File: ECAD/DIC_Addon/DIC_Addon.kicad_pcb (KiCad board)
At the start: 2 copper layers, 67.9 x 50.2 mm, 63 parts, among them J2 Conn_01x06_Pin, J3 Conn_01x06_Pin, J4 Conn_01x06_Pin, J5 Conn_01x06_Pin, Q1 FDN352AP, Q10 2N7002, Q11 2N7002, Q12 2N7002, Q2 FDN352AP, Q3 FDN352AP, Q4 FDN352AP, Q5 2N7002, Q6 2N7002, Q7 2N7002, Q8 2N7002, Q9 2N7002, U1 Thebe-II

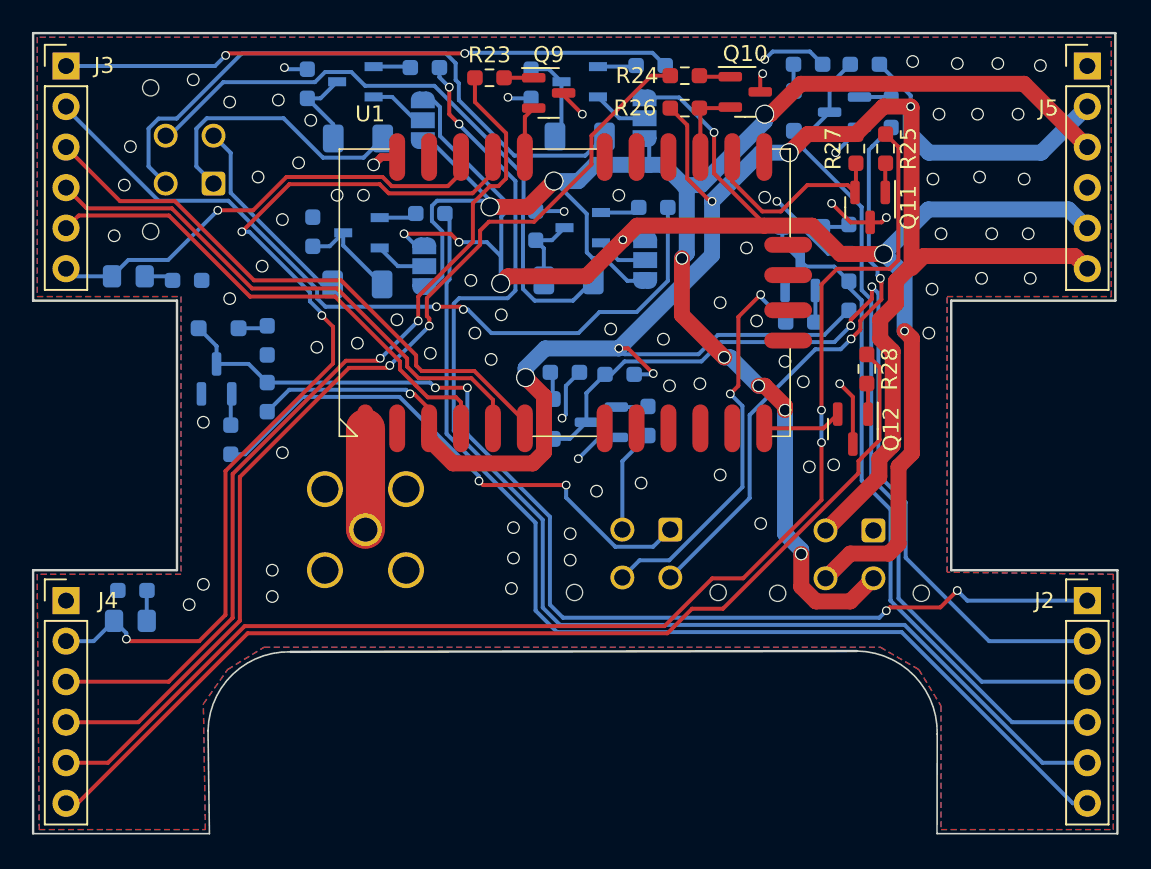
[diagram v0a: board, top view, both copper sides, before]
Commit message: switch to ribbon cable pcb interconnect
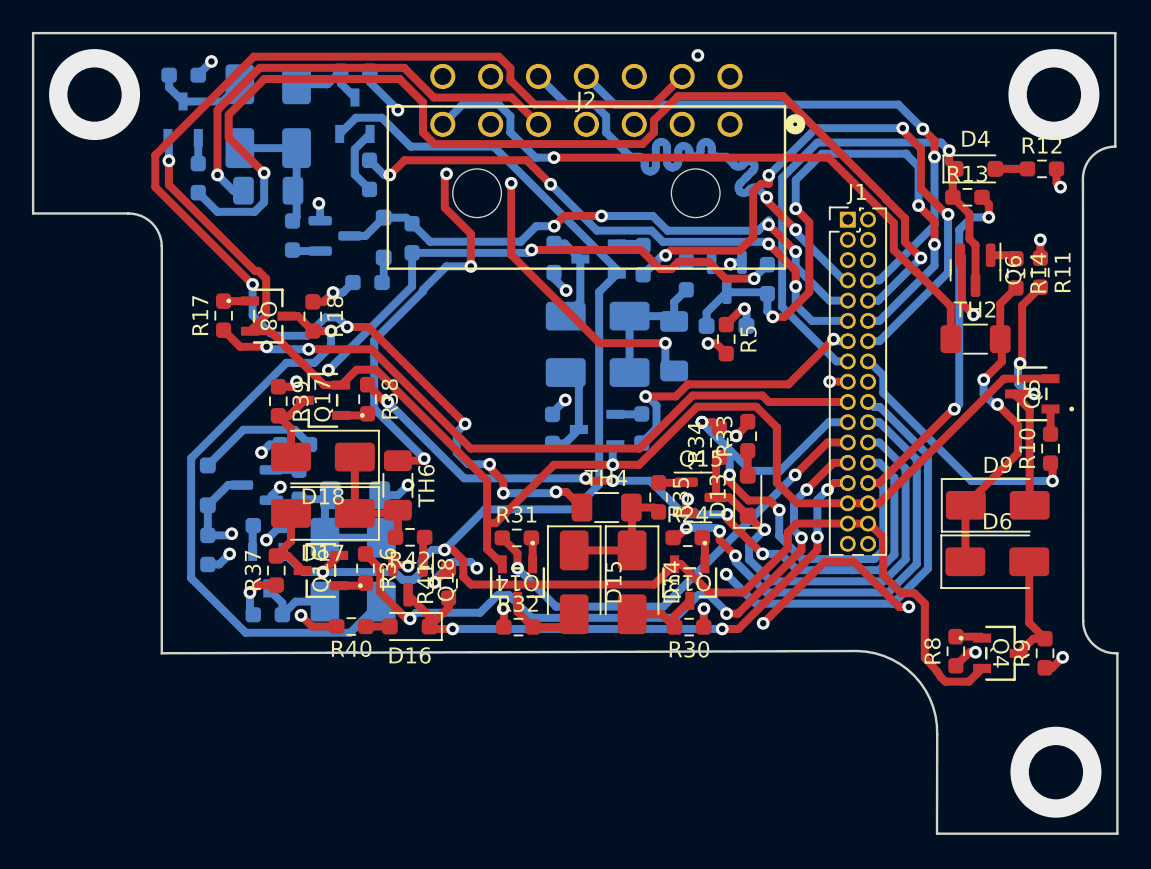
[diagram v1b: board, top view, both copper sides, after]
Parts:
- removed 868Mhz: Conn_Coaxial, Connector_Coaxial:SMA_Wurth_60312002114503_Vertical
- removed EXT_Power1, GPI1, GPO1: Micro-Fit_3.0_43045-0412, Lukas:Molex_Micro-Fit_3.0_43045-0412_2x02_P3.00mm_Vertical
- removed J3, J4, J5: Conn_01x06_Pin, Connector_PinHeader_2.54mm:PinHeader_1x06_P2.54mm_Vertical
- removed JP1, JP2, JP3, JP4: Jumper_3_Open, Jumper:SolderJumper-3_P1.3mm_Open_RoundedPad1.0x1.5mm_NumberLabels
- removed Radio_RX1, Radio_TX1: LED Blue, LED_SMD:LED_0805_2012Metric_Pad1.15x1.40mm_HandSolder
- removed U1: Thebe-II, Lukas:Thebe-II
- added D10: Z 3.3V, Diode_SMD:D_SOD-323_HandSoldering, B.Cu at (22.9, 40.3)
- added D11: B120-13-F, Diode_SMD:D_SMA, B.Cu at (30.2, 45.6)
- added D12: B120-13-F, Diode_SMD:D_SMA, B.Cu at (33.8, 45.6)
- added D13: Z 3.3V, Diode_SMD:D_SOD-323_HandSoldering, F.Cu at (56.7, 40.9)
- added D14: B120-13-F, Diode_SMD:D_SMA, F.Cu at (49.5, 46.4)
- added D15: B120-13-F, Diode_SMD:D_SMA, F.Cu at (45.8, 46.4)
- added D16: Z 3.3V, Diode_SMD:D_SOD-323_HandSoldering, F.Cu at (35.5, 49.1)
- added D17: B120-13-F, Diode_SMD:D_SMA, F.Cu at (30.1, 42.0)
- added D18: B120-13-F, Diode_SMD:D_SMA, F.Cu at (30.1, 38.5)
- added D5: Z 3.3V, Diode_SMD:D_SOD-323_HandSoldering, B.Cu at (33.9, 24.8)
- added D6: B120-13-F, Diode_SMD:D_SMA, F.Cu at (72.4, 45.1)
- added D7: B120-13-F, Diode_SMD:D_SMA, B.Cu at (28.4, 17.1)
- added D8: B120-13-F, Diode_SMD:D_SMA, B.Cu at (24.9, 17.1)
- added D9: B120-13-F, Diode_SMD:D_SMA, F.Cu at (72.4, 41.5)
- added J1: WE 62702621621, Connector_PinHeader_1.27mm:PinHeader_2x17_P1.27mm_Vertical, F.Cu at (63.0, 23.6)
- added Q13: FDN352AP, Lukas:SOT23_527AG_ONS, F.Cu at (53.1, 46.4)
- added Q14: FDN352AP, Lukas:SOT23_527AG_ONS, F.Cu at (42.3, 46.4)
- added Q15: 2N7002, Package_TO_SOT_SMD:SOT-23, F.Cu at (53.8, 41.0)
- added Q16: FDN352AP, Lukas:SOT23_527AG_ONS, F.Cu at (30.0, 45.6)
- added Q17: FDN352AP, Lukas:SOT23_527AG_ONS, F.Cu at (30.1, 34.9)
- added Q18: 2N7002, Package_TO_SOT_SMD:SOT-23, F.Cu at (35.4, 46.2)
- added R29: 1kR 0603, Resistor_SMD:R_0603_1608Metric_Pad0.98x0.95mm_HandSolder, B.Cu at (28.2, 24.6)
- added R30: 10kR 0603, Resistor_SMD:R_0603_1608Metric_Pad0.98x0.95mm_HandSolder, F.Cu at (53.0, 49.2)
- added R31: 1kR 0603, Resistor_SMD:R_0603_1608Metric_Pad0.98x0.95mm_HandSolder, F.Cu at (42.2, 43.6)
- added R32: 10kR 0603, Resistor_SMD:R_0603_1608Metric_Pad0.98x0.95mm_HandSolder, F.Cu at (42.4, 49.2)
- added R33: 100R 0603, Resistor_SMD:R_0603_1608Metric_Pad0.98x0.95mm_HandSolder, F.Cu at (56.7, 37.2)
- added R34: 1kR 0603, Resistor_SMD:R_0603_1608Metric_Pad0.98x0.95mm_HandSolder, F.Cu at (54.9, 37.6)
- added R35: 1kR 0603, Resistor_SMD:R_0603_1608Metric_Pad0.98x0.95mm_HandSolder, F.Cu at (51.1, 41.0)
- added R36: 1kR 0603, Resistor_SMD:R_0603_1608Metric_Pad0.98x0.95mm_HandSolder, F.Cu at (32.8, 45.5)
- added R37: 10kR 0603, Resistor_SMD:R_0603_1608Metric_Pad0.98x0.95mm_HandSolder, F.Cu at (27.2, 45.6)
- added R38: 1kR 0603, Resistor_SMD:R_0603_1608Metric_Pad0.98x0.95mm_HandSolder, F.Cu at (32.9, 34.9)
- added R39: 10kR 0603, Resistor_SMD:R_0603_1608Metric_Pad0.98x0.95mm_HandSolder, F.Cu at (27.3, 35.0)
- added R40: 100R 0603, Resistor_SMD:R_0603_1608Metric_Pad0.98x0.95mm_HandSolder, F.Cu at (31.9, 49.1)
- added R41: 1kR 0603, Resistor_SMD:R_0603_1608Metric_Pad0.98x0.95mm_HandSolder, F.Cu at (38.0, 46.4)
- added R42: 1kR 0603, Resistor_SMD:R_0603_1608Metric_Pad0.98x0.95mm_HandSolder, F.Cu at (35.6, 43.5)
- added TH5: SMD1206B025TF, Resistor_SMD:R_1206_3216Metric_Pad1.30x1.75mm_HandSolder, B.Cu at (26.7, 21.8)
- added TH6: SMD1206B025TF, Resistor_SMD:R_1206_3216Metric_Pad1.30x1.75mm_HandSolder, F.Cu at (34.8, 40.3)
- D2, D3: value Z 3.3V -> B120-13-F; footprint Diode_SMD:D_SOD-323_HandSoldering -> Diode_SMD:D_SMA
- D4, Q4, Q6, R12, R13, R14, R17: moved to F.Cu
- J2: value Conn_01x06_Pin -> 430451400; footprint Connector_PinHeader_2.54mm:PinHeader_1x06_P2.54mm_Vertical -> Lukas:CONN_SD-43045-001_14_MOL
- Q10, Q12, R25, R28: moved to B.Cu
- Q11, Q9: value 2N7002 -> FDN352AP; footprint Package_TO_SOT_SMD:SOT-23 -> Lukas:SOT23_527AG_ONS; moved to B.Cu
- Q3: value FDN352AP -> 2N7002; footprint Lukas:SOT23_527AG_ONS -> Package_TO_SOT_SMD:SOT-23
- Q5, Q8: value 2N7002 -> FDN352AP; footprint Package_TO_SOT_SMD:SOT-23 -> Lukas:SOT23_527AG_ONS; moved to F.Cu
- Q7: value 2N7002 -> FDN352AP; footprint Package_TO_SOT_SMD:SOT-23 -> Lukas:SOT23_527AG_ONS
- R10: value 100R 0603 -> 1kR 0603; moved to F.Cu
- R11, R9: value 100R 0603 -> 10kR 0603; moved to F.Cu
- R16, R2, R4: value 1kR 0603 -> 10kR 0603
- R18: value 1kR 0603 -> 10kR 0603; moved to F.Cu
- R19: value 1kR 0603 -> 100R 0603
- R21, R22: value 180R 0603 -> 1kR 0603
- R23, R27: value 1kR 0603 -> 10kR 0603; moved to B.Cu
- R26: value 1kR 0603 -> 100R 0603; moved to B.Cu
- R5: value 10kR 0603 -> 100R 0603; moved to F.Cu
- R6, R7: value 10kR 0603 -> 1kR 0603
- R8: value 10kR 0603 -> 1kR 0603; moved to F.Cu
- TH1, TH3: value SMD1206B050TF/15 -> SMD1206B025TF
- TH2, TH4: value SMD1206B050TF/15 -> SMD1206B025TF; moved to F.Cu
- moved R9 52.5 mm to (75.3, 50.8), turned to 90 degrees
- moved Q5 51.1 mm to (74.5, 34.5)
- moved R15 47.3 mm to (26.6, 42.8), turned to 180 degrees
- moved Q7 46.2 mm to (26.6, 45.6), turned to 0 degrees
- moved R13 45.6 mm to (70.5, 22.2), turned to 0 degrees
- moved Q11 43.4 mm to (21.3, 17.4), turned to 180 degrees
- moved R25 43.1 mm to (22.3, 21.0), turned to 90 degrees
- moved R19 42.8 mm to (28.3, 37.7), turned to 180 degrees
- moved R27 42.4 mm to (21.4, 14.6), turned to 180 degrees
- moved R16 41.5 mm to (26.6, 48.4), turned to 0 degrees
- moved R20 39.8 mm to (22.9, 44.3), turned to -90 degrees
- moved Q10 39.3 mm to (25.9, 40.3), turned to 180 degrees
- moved TH2 38.9 mm to (71.0, 31.1)
- moved R8 37.5 mm to (69.8, 50.7), turned to 90 degrees
- moved Q4 37.4 mm to (72.6, 50.8)
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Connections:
- D1 pad 1: GPI1_CTRL -> GPIO2_In
- D2 pad 1: GPI2_CTRL -> Net-(D2-K)
- D3 pad 1: GPI3_CTRL -> Net-(D2-K)
- D4 pad 1: GPI4_CTRL -> GPIO3_In
- J2 pad 1: GPI1_CTRL -> Analog1_In
- J2 pad 2: GPI2_CTRL -> Analog0_In
- J2 pad 3: GPI3_CTRL -> Analog2_In
- J2 pad 4: GPI4_CTRL -> Analog3_In
- J2 pad 5: GPO1_CTRL -> GPIO1_out/in
- J2 pad 6: GPO2_CTRL -> GPIO2_out/in
- Q1 pad 2: Net-(JP1-C) -> +12V
- Q1 pad 3: Net-(Q1-D) -> Net-(D2-A)
- Q10 pad 2: Net-(Q10-S) -> GND
- Q10 pad 3: GND -> GPIO4_In
- Q11 pad 2: Net-(Q11-S) -> +5V
- Q11 pad 3: GND -> Net-(D8-A)
- Q12 pad 2: Net-(Q12-S) -> GND
- Q12 pad 3: GND -> GPIO1_In
- Q2 pad 2: Net-(JP2-C) -> +5V
- Q2 pad 3: Net-(Q2-D) -> Net-(D3-A)
- Q3 pad 2: Net-(JP3-C) -> GND
- Q3 pad 3: Net-(Q3-D) -> GPIO2_In
- Q4 pad 2: Net-(JP4-C) -> +12V
- Q4 pad 3: Net-(Q4-D) -> Net-(D6-A)
- Q5 pad 2: GND -> +5V
- Q5 pad 3: GPI1_CTRL -> Net-(D9-A)
- Q6 pad 3: GPI2_CTRL -> GPIO3_In
- Q7 pad 2: GND -> +12V
- Q7 pad 3: GPI3_CTRL -> Net-(D11-A)
- Q8 pad 2: GND -> +5V
- Q8 pad 3: GPI4_CTRL -> Net-(D12-A)
- Q9 pad 2: Net-(Q9-S) -> +12V
- Q9 pad 3: GND -> Net-(D7-A)
- R1 pad 1: GPO1_CTRL -> GPIO2_12VOut
- R10 pad 1: Net-(D2-A) -> GPIO3_5VOut
- R10 pad 2: GND -> Net-(Q5-G)
- R11 pad 1: Net-(D3-A) -> GND
- R11 pad 2: GND -> Net-(D9-A)
- R13 pad 1: GPI1_CTRL -> GPIO3_In
- R14 pad 1: GPI2_CTRL -> Net-(Q6-G)
- R14 pad 2: +3.3V -> Net-(D6-K)
- R15 pad 1: GPI3_CTRL -> GPIO4_12VOut
- R15 pad 2: +3.3V -> Net-(Q7-G)
- R16 pad 1: GPI4_CTRL -> GND
- R16 pad 2: +3.3V -> Net-(D11-A)
- R17 pad 1: Net-(Q5-G) -> GPIO4_5VOut
- R17 pad 2: GPI1 -> Net-(Q8-G)
- R18 pad 1: Net-(Q6-G) -> GND
- R18 pad 2: GPI2 -> Net-(D12-A)
- R19 pad 1: Net-(Q7-G) -> Net-(D10-A)
- R19 pad 2: GPI3 -> GND
- R2 pad 1: GPO2_CTRL -> GND
- R2 pad 2: Net-(Q2-G) -> Net-(D2-A)
- R20 pad 1: Net-(Q8-G) -> GPIO4_In
- R20 pad 2: GPI4 -> +3.3V
- R21 pad 1: Net-(Radio_TX1-K) -> GPIO1_12VOut
- R21 pad 2: GND -> Net-(Q9-G)
- R22 pad 1: GND -> Net-(Q10-G)
- R22 pad 2: Net-(Radio_RX1-K) -> Net-(D11-K)
- R23 pad 1: Radio_RESET -> GND
- R23 pad 2: Net-(Q9-G) -> Net-(D7-A)
- R24 pad 1: Mode_1 -> GPIO5_12VOut
- R24 pad 2: Net-(Q10-G) -> Net-(Q13-G)
- R25 pad 1: Wake-Up -> GPIO1_5VOut
- R26 pad 1: Net-(Q10-S) -> Net-(D5-A)
- R26 pad 2: +3.3V -> GND
- R27 pad 1: Net-(Q11-S) -> GND
- R27 pad 2: +3.3V -> Net-(D8-A)
- R28 pad 1: Radio_BOOT -> GPIO1_In
- R28 pad 2: Net-(Q12-G) -> +3.3V
- R3 pad 1: GPO3_CTRL -> GPIO2_5VOut
- R3 pad 2: Net-(Q3-G) -> Net-(Q2-G)
- R4 pad 1: GPO4_CTRL -> GND
- R4 pad 2: Net-(Q4-G) -> Net-(D3-A)
- R5 pad 1: GND -> Net-(D1-A)
- R5 pad 2: Net-(Q1-D) -> GND
- R6 pad 1: GND -> GPIO2_In
- R6 pad 2: Net-(Q2-D) -> +3.3V
- R7 pad 1: GND -> Net-(Q3-G)
- R7 pad 2: Net-(Q3-D) -> Net-(D2-K)
- R8 pad 1: GND -> GPIO3_12VOut
- R8 pad 2: Net-(Q4-D) -> Net-(Q4-G)
- R9 pad 1: Net-(D1-A) -> GND
- R9 pad 2: GND -> Net-(D6-A)
- TH1 pad 1: GPO1 -> GPIO2_out/in
- TH1 pad 2: Net-(Q1-D) -> Net-(D2-K)
- TH2 pad 1: GPO2 -> GPIO3_out/in
- TH2 pad 2: Net-(Q2-D) -> Net-(D6-K)
- TH3 pad 1: GPO3 -> GPIO4_out/in
- TH3 pad 2: Net-(Q3-D) -> Net-(D11-K)
- TH4 pad 1: GPO4 -> GPIO5_out/in
- TH4 pad 2: Net-(Q4-D) -> Net-(D14-K)
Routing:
- net +12V: track 0.00 -> 107.2 mm, vias 0 -> 2
- net Wake-Up: track 81.4 -> 0.00 mm, vias 2 -> 0
- net GPO1_CTRL: track 79.7 -> 0.00 mm, vias 2 -> 0
- net GPIO5_out/in: track 0.00 -> 79.6 mm, vias 0 -> 6
- net +BATT: track 103.2 -> 30.0 mm, vias 7 -> 0
- net GPIO4_In: track 0.00 -> 70.1 mm, vias 0 -> 3
- net GPI1_CTRL: track 69.8 -> 0.00 mm, vias 4 -> 0
- net GPIO1_5VOut: track 0.00 -> 69.6 mm, vias 0 -> 2
- net GPO2_CTRL: track 67.0 -> 0.00 mm
- net Radio_BOOT: track 66.5 -> 0.00 mm
- net Mode_1: track 62.7 -> 0.00 mm, vias 2 -> 0
- net RX_IND: track 60.2 -> 0.00 mm, vias 3 -> 0
- net GPIO4_12VOut: track 0.00 -> 59.1 mm, vias 0 -> 2
- net GPI2_CTRL: track 57.1 -> 0.00 mm, vias 2 -> 0
- net Radio_RESET: track 55.3 -> 0.00 mm, vias 2 -> 0
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- added copper zone on In1.Cu, net GND
- added copper zone on In2.Cu, net GND
- removed copper zone on B.Cu, net GND
- removed copper zone on F.Cu, net GND
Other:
- outline, holes or cut-outs redrawn
- copper layers 2 -> 4

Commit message: finisjed PCB projekt
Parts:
- removed J1: WE 62702621621, Connector_PinHeader_1.27mm:PinHeader_2x17_P1.27mm_Vertical
- added J3: WE 62702621621, Connector_PinHeader_1.27mm:PinHeader_2x08_P1.27mm_Vertical, B.Cu at (50.6, 23.9)
- added J4: Conn_02x05_Top_Bottom, Connector_PinSocket_1.27mm:PinSocket_2x05_P1.27mm_Vertical, F.Cu at (75.8, 54.5)
- added J5: Conn_02x05_Top_Bottom, Connector_PinSocket_1.27mm:PinSocket_2x05_P1.27mm_Vertical, F.Cu at (16.1, 20.7)
- added J6: Conn_02x05_Top_Bottom, Connector_PinSocket_1.27mm:PinSocket_2x05_P1.27mm_Vertical, F.Cu at (16.9, 54.5)
- J2: value 430451400 -> Conn_02x05_Top_Bottom; footprint Lukas:CONN_SD-43045-001_14_MOL -> Connector_PinSocket_1.27mm:PinSocket_2x05_P1.27mm_Vertical
- Q8, R17, R18, R5: moved to B.Cu
- moved R27 60.7 mm to (75.9, 41.3), turned to 0 degrees
- moved Q11 58.5 mm to (75.9, 38.5), turned to 0 degrees
- moved R25 54.5 mm to (75.0, 34.8), turned to -90 degrees
- moved D8 52.2 mm to (72.4, 38.7), turned to -90 degrees
- moved D7 45.8 mm to (68.8, 38.7), turned to -90 degrees
- moved TH5 45.6 mm to (70.6, 34.0), turned to 180 degrees
- moved R12 45.6 mm to (29.9, 15.1), turned to 180 degrees
- moved R23 42.8 mm to (65.2, 41.5), turned to 0 degrees
- moved R29 41.4 mm to (69.1, 31.2), turned to -90 degrees
- moved D4 40.2 mm to (30.9, 18.3), turned to 90 degrees
- moved R11 39.8 mm to (37.4, 14.2), turned to 0 degrees
- moved Q9 39.5 mm to (65.2, 38.7), turned to 0 degrees
- moved R9 39.5 mm to (61.2, 13.9), turned to 180 degrees
- moved R13 38.0 mm to (32.6, 18.8), turned to 90 degrees
- moved R14 37.8 mm to (37.4, 15.7), turned to 0 degrees
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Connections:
- J2 pad 1: Analog1_In -> CAN1_N
- J2 pad 10: GPIO6_out/in -> Analog3_In
- J2 pad 2: Analog0_In -> CAN1_P
- J2 pad 3: Analog2_In -> Analog0_In
- J2 pad 4: Analog3_In -> GND
- J2 pad 5: GPIO1_out/in -> GND
- J2 pad 6: GPIO2_out/in -> Analog1_In
- J2 pad 7: GPIO3_out/in -> GND
- J2 pad 8: GPIO4_out/in -> Analog2_In
- J2 pad 9: GPIO5_out/in -> GND
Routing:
- net GPIO5_out/in: track 79.6 -> 33.7 mm, vias 6 -> 2
- net +5V: track 87.9 -> 130.4 mm, vias 2 -> 8
- net +BATT: track 30.0 -> 65.5 mm
- net GPIO4_In: track 70.1 -> 35.0 mm, vias 3 -> 2
- net GPIO3_out/in: track 41.2 -> 6.78 mm, vias 1 -> 0
- net GPIO4_out/in: track 53.5 -> 19.3 mm
- net GPIO3_5VOut: track 16.5 -> 46.1 mm
- net GPIO3_12VOut: track 27.6 -> 57.0 mm
- net GPIO4_12VOut: track 59.1 -> 30.2 mm
- net GPIO4_5VOut: track 43.7 -> 16.5 mm
- net GPIO2_12VOut: track 39.1 -> 14.1 mm, vias 4 -> 0
- net GPIO5_In: track 28.4 -> 52.8 mm
- net GPIO5_12VOut: track 29.0 -> 49.7 mm
- net +3.3V: track 142.4 -> 122.1 mm
- net GPIO1_12VOut: track 36.1 -> 56.3 mm, vias 4 -> 5
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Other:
- board size 67.9 x 50.2 mm -> 67.9 x 50.3 mm

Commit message: few small changes
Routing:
- net GPIO3_In: track 32.7 -> 31.1 mm
- net GPIO3_5VOut: track 46.1 -> 45.1 mm
- net GPIO3_12VOut: track 57.0 -> 56.4 mm

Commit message: production ready
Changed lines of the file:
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@@
     (property "ki_keywords" "FDN352AP")
     (attr smd)
-    (fp_text reference "Q14" (at 2.5608 -0.8858 unlocked) (layer "F.SilkS")
+    (fp_text reference "Q14" (at 0 0 -90 unlocked) (layer "F.SilkS")
         (effects (font (size 1 1) (thickness 0.15)))
     )
@@
     (property "ki_keywords" "FDN352AP")
     (attr smd)
-    (fp_text reference "Q16" (at -2.9752 -3.302 unlocked) (layer "F.SilkS")
+    (fp_text reference "Q16" (at 0 0 unlocked) (layer "F.SilkS")
         (effects (font (size 1 1) (thickness 0.15)))
     )
@@
     (property "ki_keywords" "FDN352AP")
     (attr smd)
-    (fp_text reference "Q13" (at -3.4082 0.0286 -90 unlocked) (layer "F.SilkS")
+    (fp_text reference "Q13" (at 0 0 -90 unlocked) (layer "F.SilkS")
         (effects (font (size 1 1) (thickness 0.15)))
     )
@@
     (property "ki_keywords" "FDN352AP")
     (attr smd)
-    (fp_text reference "Q17" (at 3.2732 -0.0254 unlocked) (layer "F.SilkS")
+    (fp_text reference "Q17" (at 0 0 unlocked) (layer "F.SilkS")
         (effects (font (size 1 1) (thickness 0.15)))
     )
@@
     (property "ki_keywords" "FDN352AP")
     (attr smd)
-    (fp_text reference "Q5" (at -1.524 -1.9056 unlocked) (layer "F.SilkS")
+    (fp_text reference "Q5" (at 0 0 180 unlocked) (layer "F.SilkS")
         (effects (font (size 1 1) (thickness 0.15)))
     )
@@
     (property "ki_keywords" "FDN352AP")
     (attr smd)
-    (fp_text reference "Q4" (at -2.7432 0.0133 unlocked) (layer "F.SilkS")
+    (fp_text reference "Q4" (at 0 0 unlocked) (layer "F.SilkS")
         (effects (font (size 1 1) (thickness 0.15)))
     )
@@
     (property "ki_keywords" "R res resistor")
     (attr smd)
-    (fp_text reference "R16" (at 30.918401 -44.303101) (layer "B.SilkS")
+    (fp_text reference "R16" (at 1.563 1.225 90) (layer "B.SilkS")
         (effects (font (size 1 1) (thickness 0.15)) (justify mirror))
     )
@@
     (property "ki_keywords" "FDN352AP")
     (attr smd)
-    (fp_text reference "Q9" (at -2.745901 -0.9906 -180 unlocked) (layer "B.SilkS")
+    (fp_text reference "Q9" (at 0 0 180 unlocked) (layer "B.SilkS")
         (effects (font (size 1 1) (thickness 0.15)) (justify mirror))
     )
-    (fp_text value "FDN352AP" (at 0 0 -180 unlocked) (layer "B.Fab")
+    (fp_text value "FDN352AP" (at 0 0 180 unlocked) (layer "B.Fab")
         (effects (font (size 1 1) (thickness 0.15)) (justify mirror))
     )
-    (fp_text user "${REFERENCE}" (at 0 0 -180 unlocked) (layer "B.Fab")
+    (fp_text user "${REFERENCE}" (at 0 0 180 unlocked) (layer "B.Fab")
         (effects (font (size 1 1) (thickness 0.15)) (justify mirror))
     )
@@
     (property "ki_keywords" "FDN352AP")
     (attr smd)
-    (fp_text reference "Q7" (at -2.4418 -0.0762 unlocked) (layer "B.SilkS")
+    (fp_text reference "Q7" (at 0 0 270 unlocked) (layer "B.SilkS")
         (effects (font (size 1 1) (thickness 0.15)) (justify mirror))
     )
@@
     (property "ki_keywords" "FDN352AP")
     (attr smd)
-    (fp_text reference "Q2" (at 2.547999 0.7761 unlocked) (layer "B.SilkS")
+    (fp_text reference "Q2" (at 0 0 90 unlocked) (layer "B.SilkS")
         (effects (font (size 1 1) (thickness 0.15)) (justify mirror))
     )
@@
     (property "ki_keywords" "FDN352AP")
     (attr smd)
-    (fp_text reference "Q1" (at -2.6196 0.0522 unlocked) (layer "B.SilkS")
+    (fp_text reference "Q1" (at 0 0 90 unlocked) (layer "B.SilkS")
         (effects (font (size 1 1) (thickness 0.15)) (justify mirror))
     )
@@
     (property "ki_keywords" "FDN352AP")
     (attr smd)
-    (fp_text reference "Q11" (at 2.5908 -0.127 90 unlocked) (layer "B.SilkS")
+    (fp_text reference "Q11" (at 0 0 180 unlocked) (layer "B.SilkS")
         (effects (font (size 1 1) (thickness 0.15)) (justify mirror))
     )
-    (fp_text value "FDN352AP" (at 0 0 -180 unlocked) (layer "B.Fab")
+    (fp_text value "FDN352AP" (at 0 0 180 unlocked) (layer "B.Fab")
         (effects (font (size 1 1) (thickness 0.15)) (justify mirror))
     )
-    (fp_text user "${REFERENCE}" (at 0 0 -180 unlocked) (layer "B.Fab")
+    (fp_text user "${REFERENCE}" (at 0 0 180 unlocked) (layer "B.Fab")
         (effects (font (size 1 1) (thickness 0.15)) (justify mirror))
     )
@@
     (property "ki_keywords" "FDN352AP")
     (attr smd)
-    (fp_text reference "Q8" (at 2.936 -0.3048 unlocked) (layer "B.SilkS")
+    (fp_text reference "Q8" (at 0 0 unlocked) (layer "B.SilkS")
         (effects (font (size 1 1) (thickness 0.15)) (justify mirror))
     )
